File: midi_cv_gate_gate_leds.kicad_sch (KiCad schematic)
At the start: 80 parts, among them Q10 2N3906, Q11 2N3906, Q12 2N3906, Q13 2N3906, Q14 2N3906, Q15 2N3906, Q16 2N3906, Q17 2N3906, Q18 2N3906, Q3 2N3906, Q4 2N3906, Q5 2N3906, Q6 2N3906, Q7 2N3906, Q8 2N3906, Q9 2N3906

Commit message: Fixed alignment of jacks and LEDs
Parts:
- renumbered D9 to D201, D13 to D202, D17 to D203, D21 to D204, D10 to D207, D14 to D208, D18 to D209, D22 to D210, D11 to D211, D15 to D212, D19 to D213, D23 to D214, D12 to D216, D16 to D217, D20 to D218, D24 to D219, Q3 to Q200, Q7 to Q201, Q11 to Q202, Q15 to Q203, Q4 to Q206, Q8 to Q207, Q12 to Q208, Q16 to Q209, Q5 to Q210, Q9 to Q211, Q13 to Q212, Q17 to Q213, Q6 to Q214, Q10 to Q215, Q14 to Q216, Q18 to Q217, R148 to R301, R136 to R303, R124 to R305, R112 to R307, R152 to R309, R140 to R310, R128 to R311, R116 to R312, R156 to R318, R144 to R319, R132 to R320, R120 to R321, R149 to R325, R137 to R327, R125 to R329, R113 to R331, R141 to R334, R129 to R335, R117 to R336, R153 to R337, R157 to R342, R145 to R343, R133 to R344, R121 to R345, R150 to R350, R138 to R352, R126 to R354, R114 to R356, R154 to R360, R142 to R361, R130 to R362, R118 to R363, R158 to R367, R146 to R368, R134 to R369, R122 to R370, R151 to R375, R139 to R377, R127 to R379, R115 to R381, R143 to R383, R131 to R384, R119 to R385, R155 to R387, R159 to R389, R147 to R390, R135 to R391, R123 to R392

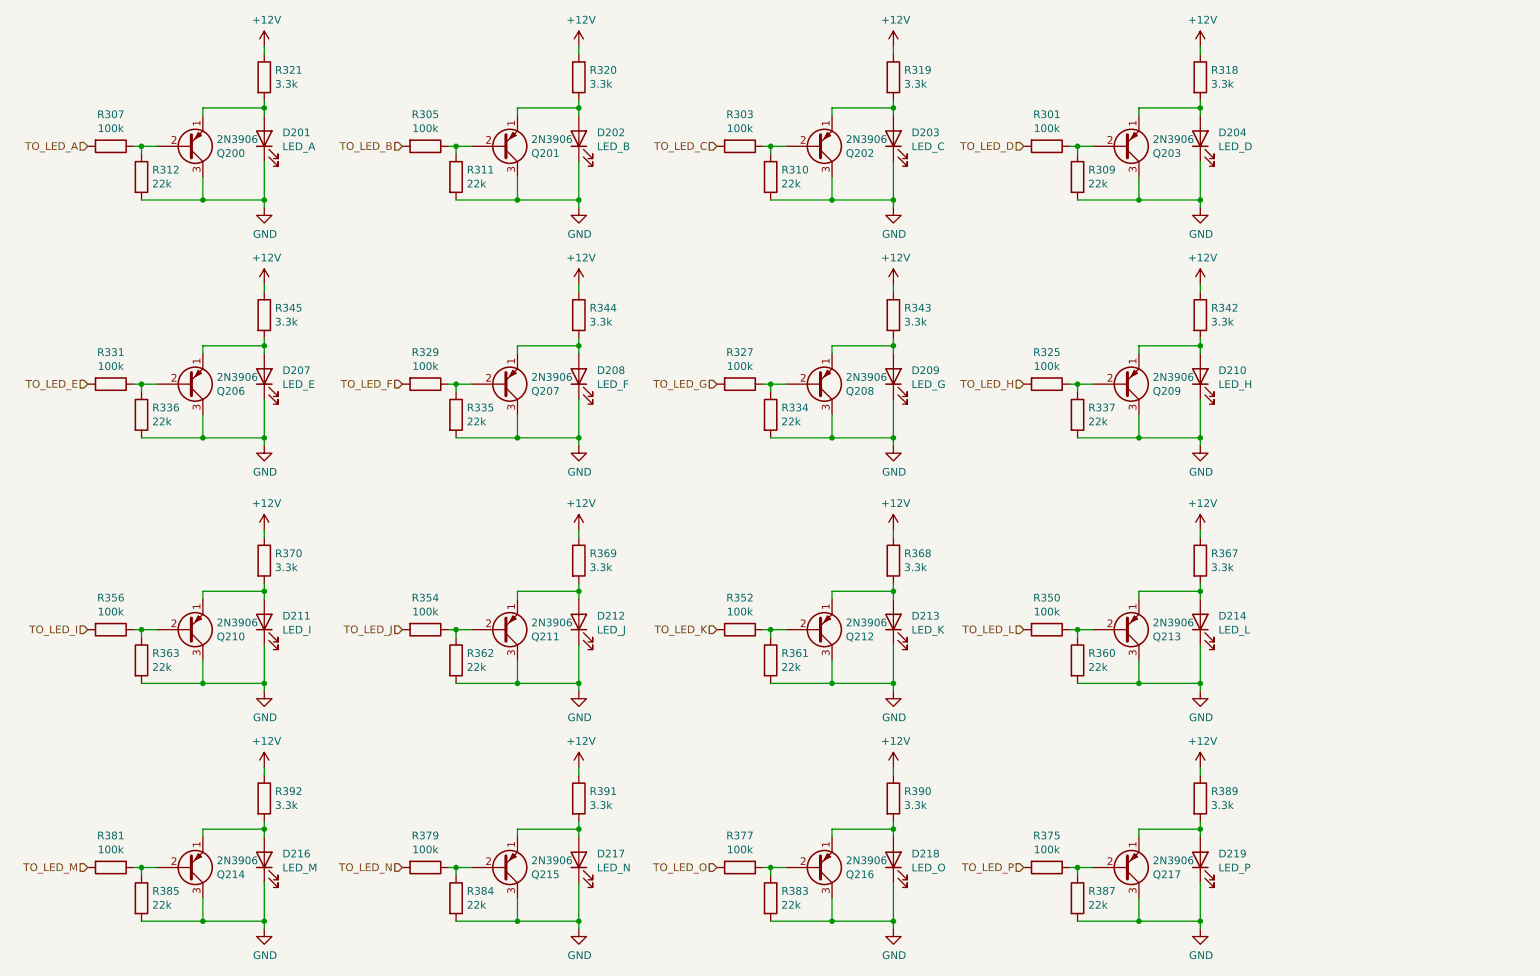
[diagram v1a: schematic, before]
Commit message: Cleanups and title blocks
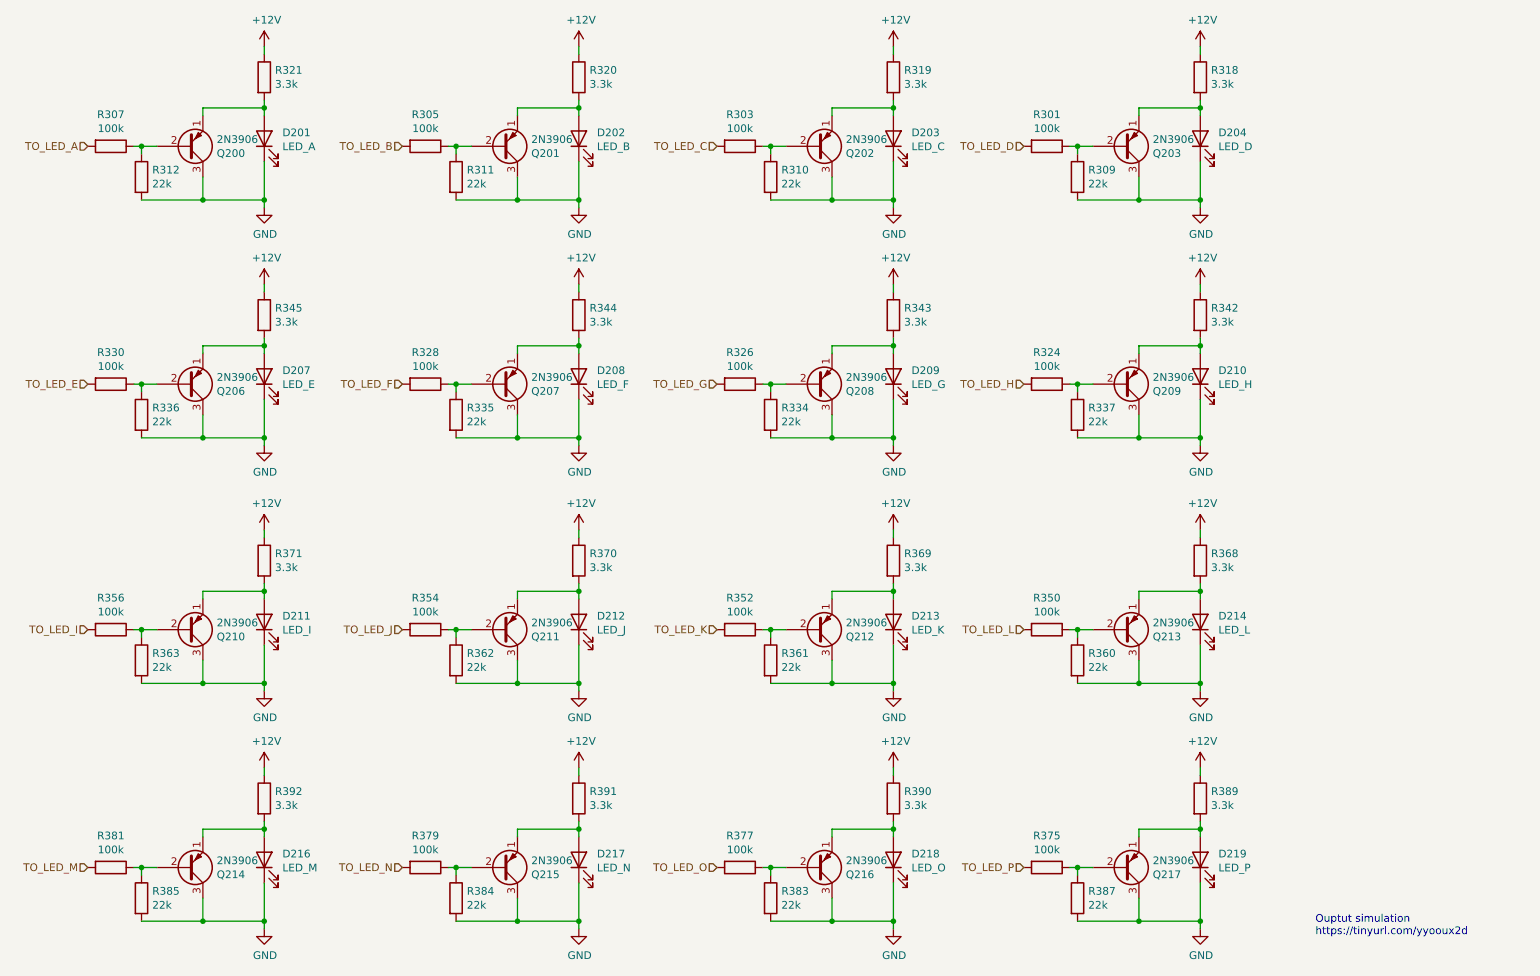
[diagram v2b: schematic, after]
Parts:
- renumbered R325 to R324, R327 to R326, R329 to R328, R331 to R330, R367 to R368, R368 to R369, R369 to R370, R370 to R371
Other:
- note added: "Ouptut simulation https://tinyurl.com/yyooux2d"
- company: (none) -> RobotDialogs
- title: (none) -> Eurorack MIDI 16x16 CV Gate
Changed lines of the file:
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@@
 (kicad_sch (version 20211123) (generator eeschema)
   (paper "A4")
+  (title_block
+    (title "Eurorack MIDI 16x16 CV Gate")
+    (date "2022-05-14")
+    (rev "1.0")
+    (company "RobotDialogs")
+  )
   (junction (at 152.4 121.92) (diameter 0) (color 0 0 0 0)
   )
@@
   (wire (pts (xy 223.52 35.56) (xy 213.36 35.56))
     (stroke (width 0) (type default) (color 0 0 0 0))
+  )
+  (text "Ouptut simulation\nhttps://tinyurl.com/yyooux2d" (at 242.57 172.72 0)
+    (effects (font (size 1.27 1.27)) (justify left bottom))
   )
   (hierarchical_label "TO_LED_G" (shape input) (at 143.51 81.28 180)
@@
   (symbol (lib_id "Device:R") (at 95.25 81.28 270) (unit 1)
     (in_bom yes) (on_board yes)
-    (property "Reference" "R329" (id 0) (at 95.25 76.0222 90))
+    (property "Reference" "R328" (id 0) (at 95.25 76.0222 90))
     (property "Value" "100k" (id 1) (at 95.25 78.3336 90))
     (property "Footprint" "Resistor_SMD:R_1206_3216Metric_Pad1.30x1.75mm_HandSolder" (id 2) (at 95.25 79.502 90)
@@
   (symbol (lib_id "Device:R") (at 147.32 81.28 270) (unit 1)
     (in_bom yes) (on_board yes)
-    (property "Reference" "R327" (id 0) (at 147.32 76.0222 90))
+    (property "Reference" "R326" (id 0) (at 147.32 76.0222 90))
     (property "Value" "100k" (id 1) (at 147.32 78.3336 90))
     (property "Footprint" "Resistor_SMD:R_1206_3216Metric_Pad1.30x1.75mm_HandSolder" (id 2) (at 147.32 79.502 90)
@@
   (symbol (lib_id "Device:R") (at 198.12 81.28 270) (unit 1)
     (in_bom yes) (on_board yes)
-    (property "Reference" "R325" (id 0) (at 198.12 76.0222 90))
+    (property "Reference" "R324" (id 0) (at 198.12 76.0222 90))
     (property "Value" "100k" (id 1) (at 198.12 78.3336 90))
     (property "Footprint" "Resistor_SMD:R_1206_3216Metric_Pad1.30x1.75mm_HandSolder" (id 2) (at 198.12 79.502 90)
@@
   (symbol (lib_id "Device:R") (at 172.72 110.49 0) (unit 1)
     (in_bom yes) (on_board yes)
-    (property "Reference" "R368" (id 0) (at 174.498 109.3216 0)
+    (property "Reference" "R369" (id 0) (at 174.498 109.3216 0)
       (effects (font (size 1.27 1.27)) (justify left))
     )
@@
   (symbol (lib_id "Device:R") (at 68.58 110.49 0) (unit 1)
     (in_bom yes) (on_board yes)
-    (property "Reference" "R370" (id 0) (at 70.358 109.3216 0)
+    (property "Reference" "R371" (id 0) (at 70.358 109.3216 0)
       (effects (font (size 1.27 1.27)) (justify left))
     )
@@
   (symbol (lib_id "Device:R") (at 120.65 110.49 0) (unit 1)
     (in_bom yes) (on_board yes)
-    (property "Reference" "R369" (id 0) (at 122.428 109.3216 0)
+    (property "Reference" "R370" (id 0) (at 122.428 109.3216 0)
       (effects (font (size 1.27 1.27)) (justify left))
     )
@@
   (symbol (lib_id "Device:R") (at 43.18 81.28 270) (unit 1)
     (in_bom yes) (on_board yes)
-    (property "Reference" "R331" (id 0) (at 43.18 76.0222 90))
+    (property "Reference" "R330" (id 0) (at 43.18 76.0222 90))
     (property "Value" "100k" (id 1) (at 43.18 78.3336 90))
     (property "Footprint" "Resistor_SMD:R_1206_3216Metric_Pad1.30x1.75mm_HandSolder" (id 2) (at 43.18 79.502 90)
@@
   (symbol (lib_id "Device:R") (at 223.52 110.49 0) (unit 1)
     (in_bom yes) (on_board yes)
-    (property "Reference" "R367" (id 0) (at 225.298 109.3216 0)
-      (effects (font (size 1.27 1.27)) (justify left))
-    )
+    (property "Reference" "R368" (id 0) (at 225.298 109.3216 0)
+      (effects (font (size 1.27 1.27)) (justify left))
+    )
